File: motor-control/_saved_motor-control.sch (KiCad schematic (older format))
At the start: 1 part

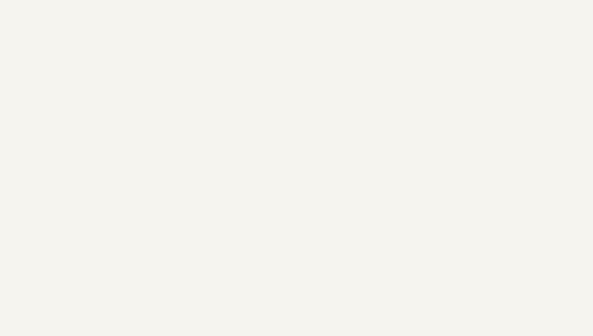
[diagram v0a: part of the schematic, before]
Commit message: Actually get rid of deleted files
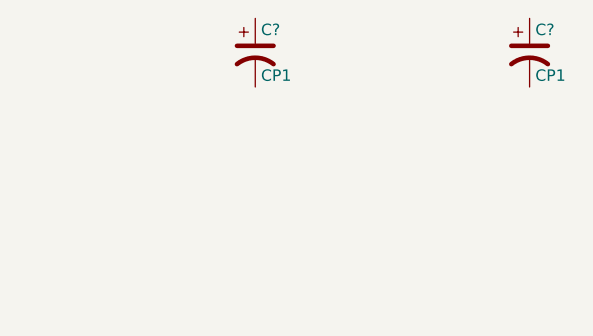
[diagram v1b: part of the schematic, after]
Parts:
- added C? (x2): CP1, symbol CP1
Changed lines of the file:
@@
+	1    0    0    -1
+$EndComp
+$Comp
+L CP1 C?
+U 1 1 5633C8D4
+P 7950 1750
+F 0 "C?" H 7975 1850 50  0000 L CNN
+F 1 "CP1" H 7975 1650 50  0000 L CNN
+F 2 "" H 7950 1750 60  0000 C CNN
+F 3 "" H 7950 1750 60  0000 C CNN
+	1    7950 1750
+	1    0    0    -1
+$EndComp
+$Comp
+L CP1 C?
+U 1 1 5633CA41
+P 9150 1750
+F 0 "C?" H 9175 1850 50  0000 L CNN
+F 1 "CP1" H 9175 1650 50  0000 L CNN
+F 2 "" H 9150 1750 60  0000 C CNN
+F 3 "" H 9150 1750 60  0000 C CNN
+	1    9150 1750
 	1    0    0    -1
 $EndComp
